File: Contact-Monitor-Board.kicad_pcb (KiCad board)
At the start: 2 copper layers, 100 x 100 mm, 82 parts, among them J1 Screw_Terminal_01x02, J10 Screw_Terminal_01x02, J11 Screw_Terminal_01x02, J12 Screw_Terminal_01x02, J13 Screw_Terminal_01x02, J14 Screw_Terminal_01x02, J15 Screw_Terminal_01x02, J16 Screw_Terminal_01x02, J2 Screw_Terminal_01x02, J3 Screw_Terminal_01x02, J4 Screw_Terminal_01x02, J5 Screw_Terminal_01x02, J6 Screw_Terminal_01x02, J7 Screw_Terminal_01x02, J8 Screw_Terminal_01x02, J9 Screw_Terminal_01x02, Q1 2N7002, Q10 2N7002, Q11 2N7002, Q12 2N7002, Q13 2N7002, Q14 2N7002, Q15 2N7002, Q16 2N7002, Q2 2N7002, Q3 2N7002, Q4 2N7002, Q5 2N7002, Q6 2N7002, Q7 2N7002, Q8 2N7002, Q9 2N7002, SW1 SW_Nidec_CAS-120A1, U1 74HC4017D, U2 TLC555CD, U3 TPS61222DCK

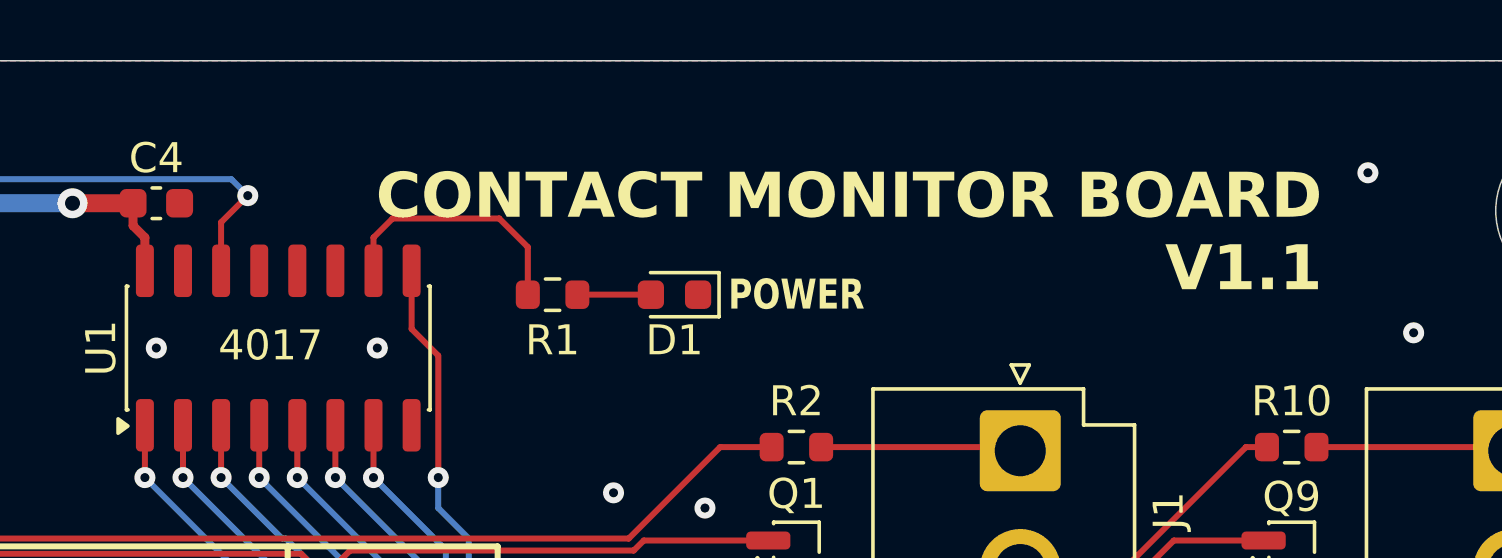
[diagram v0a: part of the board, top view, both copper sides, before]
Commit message: 接点電流と表示輝度を改善し、スキャンを9ステップ化
LED 電流制限抵抗を 1 kΩ → 470 Ω に変更。接点電流をピーク約 2.7 mA →
約 5.2 mA に引き上げ、接点酸化皮膜に対するマージンと LED の視認性を改善した。

- R18 を 1 kΩ → 4.7 kΩ に変更し、抵抗を 470 Ω / 4.7 kΩ の 2 種類に集約
- R20（4017 CLK プルアップ）を未実装化。TLC555 の出力が CMOS プッシュプル
  のため不要で、平均 0.48 mA の無駄な消費を削減
- 4017 の Q9 を MR に接続して自己リセットさせ、スキャンを 10 → 9 ステップに
  短縮。リフレッシュ 102 Hz → 113 Hz、デューティ 1/10 → 1/9
- README に「接続間違い時の動作」を追記。LED アノードを 4017 出力に接続して
  いる設計意図（VCC 直結にすると挿し間違いが誤点灯する）を明文化

Co-Authored-By: Claude Opus 5 <noreply@anthropic.com>
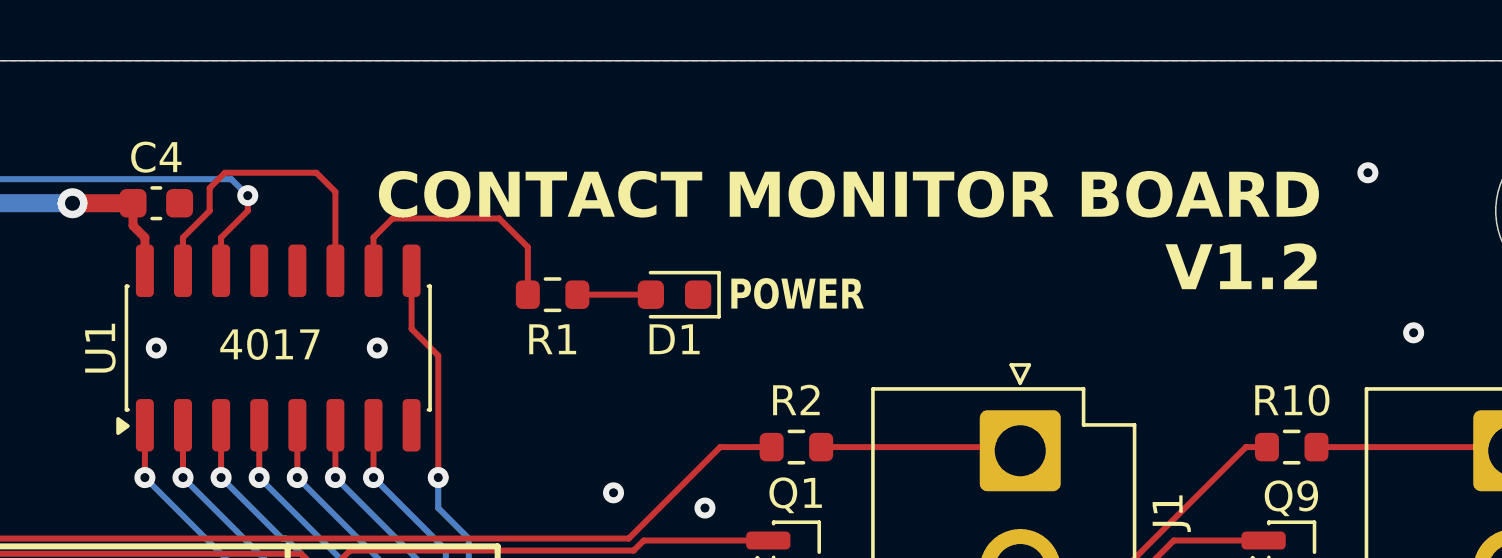
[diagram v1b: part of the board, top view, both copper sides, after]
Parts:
- R1, R10, R11, R12, R13, R14, R15, R16, R17, R2, R3, R4, R5, R6, R7, R8, R9: value 1.0k -> 470
- R18: value 1.0k -> 4.7k
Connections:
- U1 pad 11: unconnected-(U1-Q9-Pad11) -> Net-(U1-Q9)
- U1 pad 15: GND -> Net-(U1-Q9)
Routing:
- net Net-(U1-Q9): track 0.00 -> 10.4 mm
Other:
- board text added: "CONTACT MONITOR BOARD V1.2"
- board text added: "CONTACT MONITOR BOARD v1.2 2026-08 (C) 2026 SATORU YAMAGUCHI CERN-OHL-P v2"
- board text removed: "CONTACT MONITOR BOARD V1.1"
- board text removed: "CONTACT MONITOR BOARD v1.0 2026-08 (C) 2026 SATORU YAMAGUCHI CERN-OHL-P v2"

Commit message: V1.3 公開に向けて設計データとドキュメントを整備
シルク:
- 警告文から Markdown 記法 [!WARNING] を除去し WARNING: に変更
- 裏面シルク回路図のリファレンス範囲を修正
  (D2-D14 -> D2-D17 / R2-R14 -> R2-R17 / J1-J13 -> J1-J16 / Q1-Q13 -> Q1-Q16)

基板・回路図:
- 観測用ヘッダ J17 (GND / +5V / CLK / RST、DNP) を追加
- 電源部のリレイアウトと、残っていた dangling via の除去 (DRC 0 件)
- PWR_FLAG を電池側へ移して ERC エラーを解消し、
  SW1 のフットプリント差分と U3 の L ピンを除外設定に登録
- 回路図タイトルブロックの日付を更新

製造データ:
- BOM/CPL の部品名を実発注品に合わせて修正
  (Screw_Terminal_01x02 -> JST VH 02 / SW_Nidec_CAS-120A1 -> KH-SS12D01-G3-5.0 /
   VALUE -> BH-AAA-A1AJ001)
- ガーバー・BOM・CPL・回路図 PDF を再生成

README:
- 電池の極性に関する警告を追加 (逆接保護回路なし)
- 観測用ヘッダ J17 の説明を追加

Co-Authored-By: Claude Opus 5 <noreply@anthropic.com>
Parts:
- added J17: header 4, Connector_PinHeader_2.54mm:PinHeader_1x04_P2.54mm_Vertical, F.Cu at (92.6, 37.2)
- BT1: value VALUE -> BH-AAA-A1AJ001
- J1, J10, J11, J12, J13, J14, J15, J16, J2, J3, J4, J5, J6, J7, J8, J9: value Screw_Terminal_01x02 -> JST VH 02
- SW1: value SW_Nidec_CAS-120A1 -> KH-SS12D01-G3-5.0
- moved C1 16.8 mm to (107.8, 42.3)
- moved C2 16.8 mm to (114.2, 39.3)
- moved C3 16.8 mm to (114.2, 37.8)
- moved R18 16.8 mm to (109.9, 39.3)
- moved R19 16.8 mm to (111.1, 37.8)
- moved R20 16.8 mm to (115.5, 44.9)
- moved U2 16.8 mm to (111.4, 43.8)
- moved R1 3.97 mm to (128.4, 37.8)
- moved C4 2.54 mm to (120.3, 37.8)
- moved U1 2.54 mm to (124.4, 42.6)
- moved D1 2.30 mm to (134.8, 38.5)
- moved C5 1.27 mm to (83.5, 41.3)
- moved L1 1.27 mm to (85.0, 37.4)
- moved C6 1.27 mm to (88.5, 40.8)
- moved U3 1.27 mm to (86.0, 40.5)
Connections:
- net Net-(U1-CLK) renamed /CLK
- net Net-(U1-Q9) renamed /RST
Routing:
- net /RST: track 10.4 -> 36.7 mm, vias 0 -> 1
- net VCC: track 62.9 -> 73.4 mm
- net /POWER_CHECK: track 8.50 -> 2.28 mm
- net Net-(SW1-B): track 19.5 -> 25.3 mm
- net /CLK: track 34.5 -> 39.7 mm
- net Net-(D1-A): track 2.45 -> 5.04 mm
- net /BLOCK15: track 140.4 -> 142.2 mm
- net /BLOCK1: track 125.1 -> 126.4 mm
- net /BLOCK11: track 138.8 -> 137.5 mm
- net /BLOCK14: track 132.0 -> 131.0 mm
- net /BLOCK16: track 150.2 -> 149.2 mm
- net Net-(D11-K): track 31.8 -> 32.5 mm
- net /BLOCK5: track 125.4 -> 124.8 mm
- net GND: vias 64 -> 84
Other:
- board text added: "+"
- board text added: "+5V"
- board text added: "-"
- board text added: "CLK"
- board text added: "CONTACT MONITOR BOARD"
- board text added: "CONTACT MONITOR BOARD v1.3 2026-08 (C) 2026 SATORU YAMAGUCHI CERN-OHL-P v2"
- board text added: "GND"
- board text added: "RST"
- board text added: "WARNING: DRY CONTACT ONLY"
- board text added: "WARNING: WRONG POLARITY MAY CAUSE OVERHEATING OR LEAKAGE"
- board text removed: "CONTACT MONITOR BOARD V1.2"
- board text removed: "CONTACT MONITOR BOARD v1.2 2026-08 (C) 2026 SATORU YAMAGUCHI CERN-OHL-P v2"
